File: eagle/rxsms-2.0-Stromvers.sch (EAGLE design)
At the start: 17 parts, among them Q1 FDD4141TO252

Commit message: Added logos, added ordering codes, otherwise minor changes
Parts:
- LED1: OC_RS (none) -> 692-0957
- SV1: OC_FARNELL (none) -> 1096983 (Gegenstück: 1200506 oder 1097038)
- X4: OC_FARNELL (none) -> 1207598 + 2x 1855027
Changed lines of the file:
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@@
 <parts>
 <part name="FRAME4" library="frames" deviceset="DINA4_L" device=""/>
-<part name="X4" library="con-subd" deviceset="F15HP" device=""/>
-<part name="SV1" library="con-harting-ml" deviceset="ML26" device="L"/>
+<part name="X4" library="con-subd" deviceset="F15HP" device="">
+<attribute name="OC_FARNELL" value="1207598 + 2x 1855027"/>
+</part>
+<part name="SV1" library="con-harting-ml" deviceset="ML26" device="L">
+<attribute name="OC_FARNELL" value="1096983 (Gegenstück: 1200506 oder 1097038)"/>
+</part>
 <part name="FRAME8" library="frames" deviceset="DINA4_L" device=""/>
 <part name="P+13" library="supply1" deviceset="+24V" device="" value="+28V_SUPPLY"/>
@@
 </part>
 <part name="R3" library="rcl" deviceset="R-EU_" device="R0805" value="1k"/>
-<part name="LED1" library="led" deviceset="LED" device="CHIPLED_0805"/>
+<part name="LED1" library="led" deviceset="LED" device="CHIPLED_0805">
+<attribute name="OC_RS" value="692-0957"/>
+</part>
 <part name="U$1" library="light-pipe" deviceset="RLP1-200-500" device=""/>
 <part name="SJ1" library="jumper" deviceset="SJ" device=""/>
@@
 </instance>
 <instance part="R3" gate="G$1" x="172.72" y="99.06"/>
-<instance part="LED1" gate="G$1" x="182.88" y="93.98"/>
+<instance part="LED1" gate="G$1" x="182.88" y="93.98">
+<attribute name="OC_RS" x="182.88" y="93.98" size="1.778" layer="96" display="off"/>
+</instance>
 <instance part="U$1" gate="G$1" x="43.18" y="35.56"/>
 <instance part="SJ1" gate="1" x="71.12" y="132.08"/>

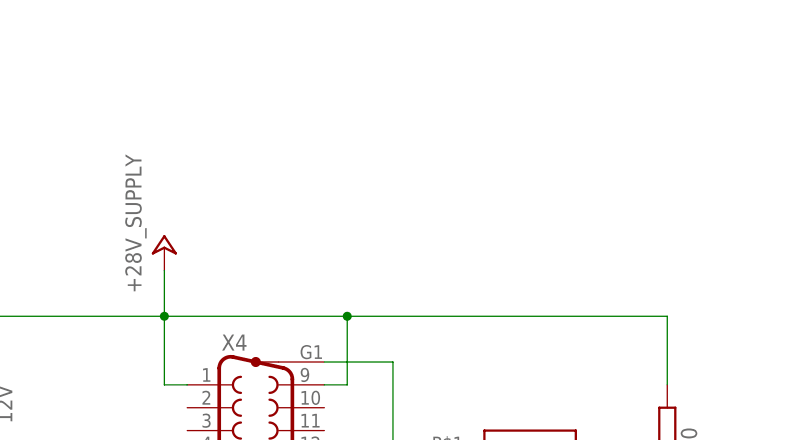
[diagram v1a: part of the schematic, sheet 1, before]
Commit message: add screws to power PCB
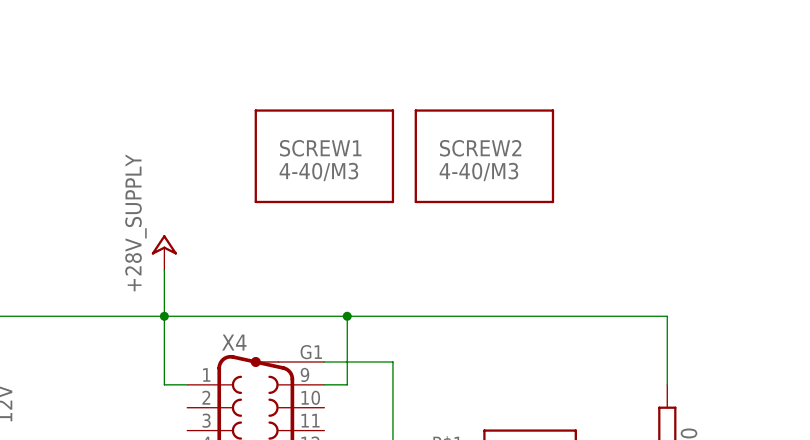
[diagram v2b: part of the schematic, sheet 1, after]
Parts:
- X4: OC_FARNELL 1207598 + 2x 1855027 -> 1207598
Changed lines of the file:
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@@
 <?xml version="1.0" encoding="utf-8"?>
 <!DOCTYPE eagle SYSTEM "eagle.dtd">
-<eagle version="6.5.0">
+<eagle version="6.6.0">
 <drawing>
 <settings>
@@
 <layer number="97" name="Info" color="7" fill="1" visible="yes" active="yes"/>
 <layer number="98" name="Guide" color="6" fill="1" visible="yes" active="yes"/>
+<layer number="99" name="SpiceOrder" color="5" fill="1" visible="yes" active="yes"/>
 <layer number="200" name="200bmp" color="7" fill="1" visible="yes" active="yes"/>
 </layers>
@@
 <part name="FRAME4" library="frames" deviceset="DINA4_L" device=""/>
 <part name="X4" library="con-subd" deviceset="F15HP" device="">
-<attribute name="OC_FARNELL" value="1207598 + 2x 1855027"/>
+<attribute name="OC_FARNELL" value="1207598"/>
 </part>
 <part name="SV1" library="con-harting-ml" deviceset="ML26" device="L">
@@
 <part name="SJ2" library="jumper" deviceset="SJ" device=""/>
 <part name="SJ3" library="jumper" deviceset="SJ" device=""/>
+<part name="SCREW1" library="dsub-mounting-screw" deviceset="DSUB_MOUNTING_SCREW" device="" value="4-40/M3">
+<attribute name="OC_FARNELL" value="4218061"/>
+</part>
+<part name="SCREW2" library="dsub-mounting-screw" deviceset="DSUB_MOUNTING_SCREW" device="" value="4-40/M3">
+<attribute name="OC_FARNELL" value="4218061"/>
+</part>
 </parts>
 <sheets>
@@
 <instance part="SJ2" gate="1" x="71.12" y="139.7"/>
 <instance part="SJ3" gate="1" x="71.12" y="147.32"/>
+<instance part="SCREW1" gate="G$1" x="121.92" y="137.16">
+<attribute name="OC_FARNELL" x="121.92" y="137.16" size="1.778" layer="96" display="off"/>
+</instance>
+<instance part="SCREW2" gate="G$1" x="139.7" y="137.16">
+<attribute name="OC_FARNELL" x="139.7" y="137.16" size="1.778" layer="96" display="off"/>
+</instance>
 </instances>
 <busses>

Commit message: fix schematics and layout
  o add a dummy package (circle) to the screw. without package, it does not
    appear in the BOM
  o update the order code for the screw: new model is a bit longer but
    much cheaper which is important because of the high number of pieces.
  o synchronize/update the screws in the layout files
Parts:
- added SCREW1, SCREW2: 4-40/M3, dsub-mounting-screw:DSUB_MOUNTING_SCREW
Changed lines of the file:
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@@
 <part name="SJ3" library="jumper" deviceset="SJ" device=""/>
 <part name="SCREW1" library="dsub-mounting-screw" deviceset="DSUB_MOUNTING_SCREW" device="" value="4-40/M3">
-<attribute name="OC_FARNELL" value="4218061"/>
+<attribute name="OC_FARNELL" value="2135988"/>
 </part>
 <part name="SCREW2" library="dsub-mounting-screw" deviceset="DSUB_MOUNTING_SCREW" device="" value="4-40/M3">
-<attribute name="OC_FARNELL" value="4218061"/>
+<attribute name="OC_FARNELL" value="2135988"/>
 </part>
 </parts>
